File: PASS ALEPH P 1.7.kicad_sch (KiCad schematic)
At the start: 73 parts, among them Q1 BCX56-16,115, Q10 BCX56-16,115, Q2 BCX53-16,115, Q3 610, Q4 610, Q5 9610, Q6 9610, Q7 610, Q8 610, Q9 BCX53-16,115

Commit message: 6 layer-board, layout finished
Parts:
- removed Q1, Q10: BCX56-16,115, 3rd package:BCX56-16,115, symbol generic components:Transistor_NPN
- added Q11, Q12: BCP56-16,115, cus_transistor:BCP56-16,115, symbol cus_transistor:BCP56-16,115
- C7, C9: footprint 3rd package:MES104J2A-7-50R0 -> cus_capacitor:MES104J2A-7-50R0
- CN1: symbol connectors:2线焊盘 -> cus_connector:2线焊盘
- CN2, CN3: symbol connectors:3线焊盘 -> cus_connector:3线焊盘
- Q2, Q9: footprint 3rd package:BCX53-16,115 -> cus_transistor:BCP53-16,115; symbol generic components:Transistor_PNP -> cus_transistor:BCP53-16,115
- Q3, Q4, Q7, Q8: value 610 -> IRF610PBF; footprint 3rd package:IRF610PBF -> cus_mosfet:IRF610PBF; symbol generic components:Mosfet_N_Channel -> cus_mosfet:IRF610PBF
- Q5, Q6: value 9610 -> IRF9610PBF; footprint 3rd package:IRF9610PBF -> cus_mosfet:IRF9610PBF; symbol generic components:Mosfet_P_Channel -> cus_mosfet:IRF9610PBF
- R1, R37: value 0 -> 10K
- R14, R23, R38: footprint generic package:R_1206 -> generic package:R 2512
- R15, R24: value 33.1 -> 33.2; footprint generic package:R_1206 -> generic package:R 2512
- R18, R21, R35, R4: footprint generic package:R_1206 -> cus_resistor:R_MELF_0207
- R19: footprint generic package:R_1206 -> cus_resistor:R_2512
- Z1: renamed from ZD1; value ZMY9V1-GS08 -> 1SMB5924BT3G; footprint 3rd package:ZMY9V1-GS08 -> cus_zener:1SMB5924BT3G; symbol generic components:Zener_Diode -> cus_zener:1SMB5924BT3G
- Z2: renamed from ZD2; value ZMY9V1-GS08 -> 1SMB5924BT3G; footprint 3rd package:ZMY9V1-GS08 -> cus_zener:1SMB5924BT3G; symbol generic components:Zener_Diode -> cus_zener:1SMB5924BT3G
- Z3: renamed from ZD3; value ZMY9V1-GS08 -> 1SMB5924BT3G; footprint 3rd package:ZMY9V1-GS08 -> cus_zener:1SMB5924BT3G; symbol generic components:Zener_Diode -> cus_zener:1SMB5924BT3G
- Z4: renamed from ZD4; value ZMY9V1-GS08 -> 1SMB5924BT3G; footprint 3rd package:ZMY9V1-GS08 -> cus_zener:1SMB5924BT3G; symbol generic components:Zener_Diode -> cus_zener:1SMB5924BT3G
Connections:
- net GND: now also Q11.3 (E), Q12.3 (E)
- net at R10.1, R2.1: now also Q11.2 (C)
- net at R11.1: now also Q11.1 (B)
- net at R29.2, R36.2: now also Q12.2 (C)
- net at R30.2: now also Q12.1 (B)

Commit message: replace some film resistor, fix some bug
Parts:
- R1, R16, R2, R22, R36, R37: footprint generic package:R_1206 -> cus_resistor:R_MELF_0207
- R14, R23: value 22.1 -> 22; footprint generic package:R 2512 -> cus_resistor:R_MELF_0207
- R15, R24: value 33.2 -> 33; footprint generic package:R 2512 -> cus_resistor:R_MELF_0207
- R38: footprint generic package:R 2512 -> cus_resistor:R_MELF_0207
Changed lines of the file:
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@@
 			)
 		)
-		(property "Footprint" "generic package:R_1206"
+		(property "Footprint" "cus_resistor:R_MELF_0207"
 			(at 34.29 96.52 0)
 			(effects
@@
 			)
 		)
-		(property "Footprint" "generic package:R_1206"
+		(property "Footprint" "cus_resistor:R_MELF_0207"
 			(at 212.09 97.79 0)
 			(effects
@@
 			)
 		)
-		(property "Footprint" "generic package:R_1206"
+		(property "Footprint" "cus_resistor:R_MELF_0207"
 			(at 208.28 68.58 0)
 			(effects
@@
 			)
 		)
-		(property "Value" "33.2"
+		(property "Value" "33"
 			(at 105.41 144.7799 0)
 			(effects
@@
 			)
 		)
-		(property "Footprint" "generic package:R 2512"
+		(property "Footprint" "cus_resistor:R_MELF_0207"
 			(at 102.87 143.51 0)
 			(effects
@@
 			)
 		)
-		(property "Footprint" "generic package:R_1206"
+		(property "Footprint" "cus_resistor:R_MELF_0207"
 			(at 143.51 88.9 0)
 			(effects
@@
 			)
 		)
-		(property "Footprint" "generic package:R 2512"
+		(property "Footprint" "cus_resistor:R_MELF_0207"
 			(at 213.36 35.56 0)
 			(effects
@@
 			)
 		)
-		(property "Footprint" "generic package:R_1206"
+		(property "Footprint" "cus_resistor:R_MELF_0207"
 			(at 40.64 68.58 0)
 			(effects
@@
 			)
 		)
-		(property "Value" "22.1"
+		(property "Value" "22"
 			(at 151.13 52.0699 0)
 			(effects
@@
 			)
 		)
-		(property "Footprint" "generic package:R 2512"
+		(property "Footprint" "cus_resistor:R_MELF_0207"
 			(at 148.59 50.8 0)
 			(effects
@@
 			)
 		)
-		(property "Value" "22.1"
+		(property "Value" "22"
 			(at 105.41 52.0699 0)
 			(effects
@@
 			)
 		)
-		(property "Footprint" "generic package:R 2512"
+		(property "Footprint" "cus_resistor:R_MELF_0207"
 			(at 102.87 50.8 0)
 			(effects
@@
 			)
 		)
-		(property "Value" "33.2"
+		(property "Value" "33"
 			(at 151.13 144.7799 0)
 			(effects
@@
 			)
 		)
-		(property "Footprint" "generic package:R 2512"
+		(property "Footprint" "cus_resistor:R_MELF_0207"
 			(at 148.59 143.51 0)
 			(effects
@@
 			)
 		)
-		(property "Footprint" "generic package:R_1206"
+		(property "Footprint" "cus_resistor:R_MELF_0207"
 			(at 104.14 88.9 0)
 			(effects

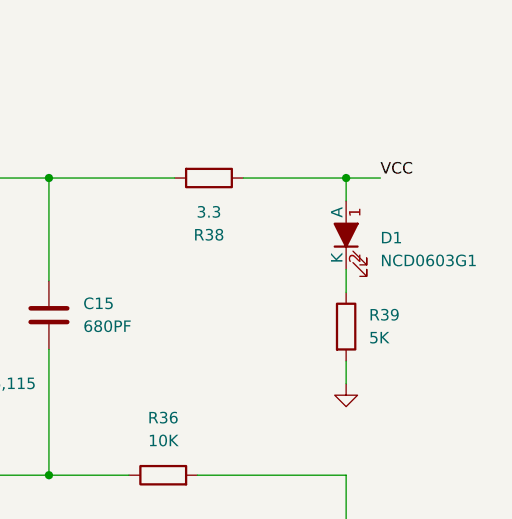
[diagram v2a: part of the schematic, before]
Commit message: use smd led
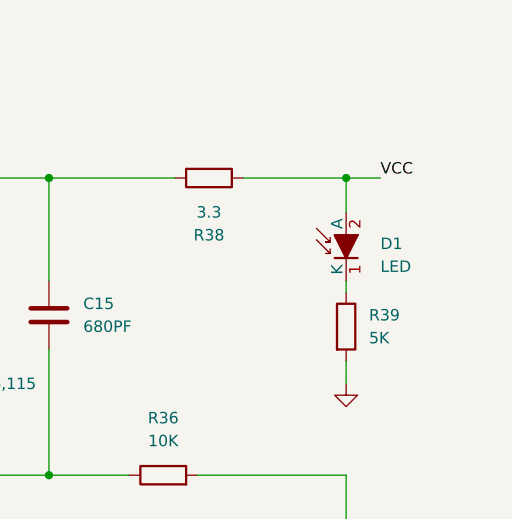
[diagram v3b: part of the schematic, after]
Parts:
- D1: value NCD0603G1 -> LED; footprint generic package:LED -> generic package:LED_1206
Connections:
- net VCC: now also D1.2 (A); no longer D1.1 (A)
- net at R39.1: now also D1.1 (K); no longer D1.2 (K)
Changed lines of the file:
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@@
 	)
 	(junction
+		(at 228.6 35.56)
+		(diameter 0)
+		(color 0 0 0 0)
+	)
+	(junction
 		(at 181.61 76.2)
 		(diameter 0)
@@
 	)
 	(junction
-		(at 228.6 35.56)
-		(diameter 0)
-		(color 0 0 0 0)
-	)
-	(junction
 		(at 123.19 95.25)
 		(diameter 0)
@@
 	(wire
 		(pts
-			(xy 217.17 35.56) (xy 228.6 35.56)
-		)
-		(stroke
-			(width 0)
-			(type default)
-		)
-	)
-	(wire
-		(pts
 			(xy 114.3 45.72) (xy 114.3 48.26)
 		)
@@
 	(wire
 		(pts
+			(xy 217.17 35.56) (xy 228.6 35.56)
+		)
+		(stroke
+			(width 0)
+			(type default)
+		)
+	)
+	(wire
+		(pts
 			(xy 91.44 104.14) (xy 95.25 104.14)
 		)
@@
 	(wire
 		(pts
-			(xy 228.6 45.72) (xy 228.6 48.26)
-		)
-		(stroke
-			(width 0)
-			(type default)
-		)
-	)
-	(wire
-		(pts
 			(xy 184.15 128.27) (xy 184.15 132.08)
 		)
@@
 	(wire
 		(pts
+			(xy 228.6 46.99) (xy 228.6 48.26)
+		)
+		(stroke
+			(width 0)
+			(type default)
+		)
+	)
+	(wire
+		(pts
 			(xy 50.8 96.52) (xy 63.5 96.52)
 		)
@@
 	(wire
 		(pts
+			(xy 228.6 35.56) (xy 232.41 35.56)
+		)
+		(stroke
+			(width 0)
+			(type default)
+		)
+	)
+	(wire
+		(pts
 			(xy 171.45 106.68) (xy 171.45 109.22)
 		)
@@
 	(wire
 		(pts
-			(xy 228.6 35.56) (xy 228.6 38.1)
-		)
-		(stroke
-			(width 0)
-			(type default)
-		)
-	)
-	(wire
-		(pts
 			(xy 40.64 96.52) (xy 50.8 96.52)
 		)
@@
 	(wire
 		(pts
-			(xy 92.71 179.07) (xy 99.06 179.07)
+			(xy 228.6 35.56) (xy 228.6 39.37)
 		)
 		(stroke
@@
 	(wire
 		(pts
-			(xy 127 22.86) (xy 114.3 22.86)
+			(xy 92.71 179.07) (xy 99.06 179.07)
 		)
 		(stroke
@@
 	(wire
 		(pts
-			(xy 148.59 116.84) (xy 148.59 123.19)
+			(xy 127 22.86) (xy 114.3 22.86)
 		)
 		(stroke
@@
 	(wire
 		(pts
-			(xy 148.59 133.35) (xy 148.59 137.16)
+			(xy 148.59 116.84) (xy 148.59 123.19)
 		)
 		(stroke
@@
 	(wire
 		(pts
-			(xy 102.87 59.69) (xy 102.87 63.5)
+			(xy 148.59 133.35) (xy 148.59 137.16)
 		)
 		(stroke
@@
 	(wire
 		(pts
-			(xy 125.73 153.67) (xy 125.73 158.75)
+			(xy 102.87 59.69) (xy 102.87 63.5)
 		)
 		(stroke
@@
 	(wire
 		(pts
-			(xy 228.6 35.56) (xy 232.41 35.56)
+			(xy 125.73 153.67) (xy 125.73 158.75)
 		)
 		(stroke
@@
 	(symbol
 		(lib_id "generic components:LED")
-		(at 228.6 41.91 270)
+		(at 228.6 43.18 90)
 		(unit 1)
 		(exclude_from_sim no)
@@
 		(fields_autoplaced yes)
 		(property "Reference" "D1"
-			(at 232.41 42.2274 90)
+			(at 232.41 42.8624 90)
 			(effects
 				(font
 					(size 1.27 1.27)
 				)
-				(justify left)
+				(justify right)
 			)
 		)
-		(property "Value" "NCD0603G1"
-			(at 232.41 44.7674 90)
+		(property "Value" "LED"
+			(at 232.41 45.4024 90)
 			(effects
 				(font
 					(size 1.27 1.27)
 				)
-				(justify left)
+				(justify right)
 			)
 		)
-		(property "Footprint" "generic package:LED"
-			(at 228.6 41.91 0)
+		(property "Footprint" "generic package:LED_1206"
+			(at 228.6 43.18 0)
 			(effects
 				(font
@@
 		)
 		(property "Datasheet" ""
-			(at 228.6 41.91 0)
+			(at 228.6 43.18 0)
 			(effects
 				(font
@@
 		)
 		(property "Description" "5MM LED BLUE 20MA 3V"
-			(at 224.282 41.91 0)
+			(at 232.918 43.18 0)
 			(effects
 				(font

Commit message: fix some bugs
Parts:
- C1, C15, C16, C2: footprint 3rd package:MMKP681K3A1001 -> cus_capacitor:B83C681JN1B0120090050EOY
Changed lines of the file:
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@@
 			)
 		)
-		(property "Footprint" "3rd package:MMKP681K3A1001"
+		(property "Footprint" "cus_capacitor:B83C681JN1B0120090050EOY"
 			(at 191.77 82.2452 0)
 			(effects
@@
 			)
 		)
-		(property "Footprint" "3rd package:MMKP681K3A1001"
+		(property "Footprint" "cus_capacitor:B83C681JN1B0120090050EOY"
 			(at 199.39 49.8348 0)
 			(effects
@@
 			)
 		)
-		(property "Footprint" "3rd package:MMKP681K3A1001"
+		(property "Footprint" "cus_capacitor:B83C681JN1B0120090050EOY"
 			(at 53.34 51.1048 0)
 			(effects
@@
 			)
 		)
-		(property "Footprint" "3rd package:MMKP681K3A1001"
+		(property "Footprint" "cus_capacitor:B83C681JN1B0120090050EOY"
 			(at 63.5 81.5848 0)
 			(effects
